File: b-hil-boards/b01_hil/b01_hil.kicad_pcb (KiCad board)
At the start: 2 copper layers, 61.7 x 30.5 mm, 40 parts, among them J1 USB_C_Receptacle_USB2.0, J2 Conn_01x03_Male, U1 ADUM4160, U2 MAX485E, U3 CH340G, Y1 Crystal

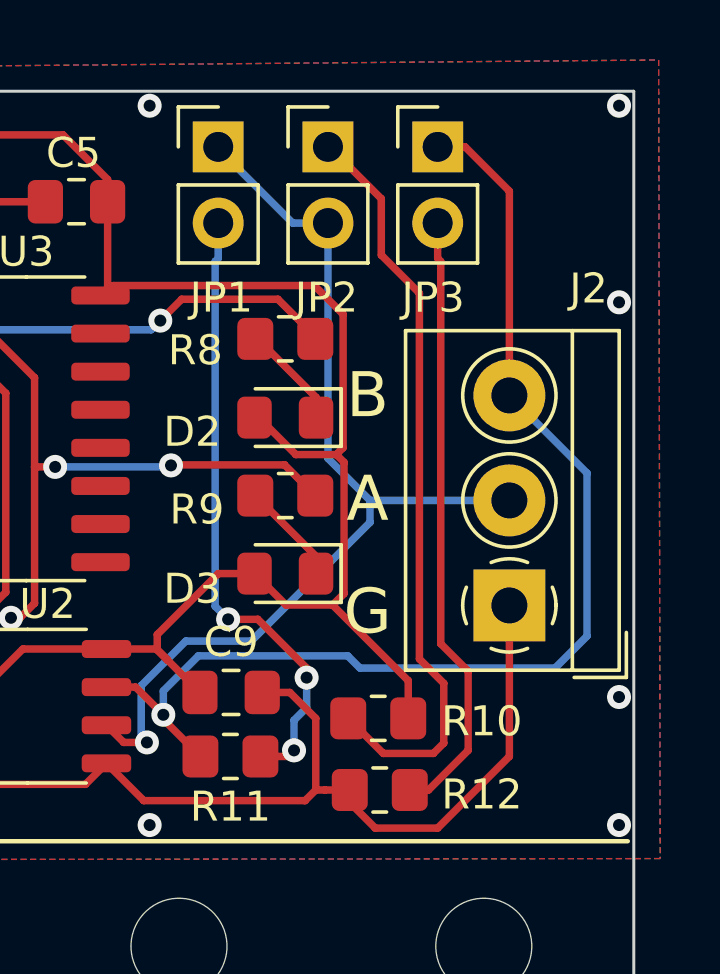
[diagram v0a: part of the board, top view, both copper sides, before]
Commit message: Changed jumper distances to be compatible with 2.54 pin headers
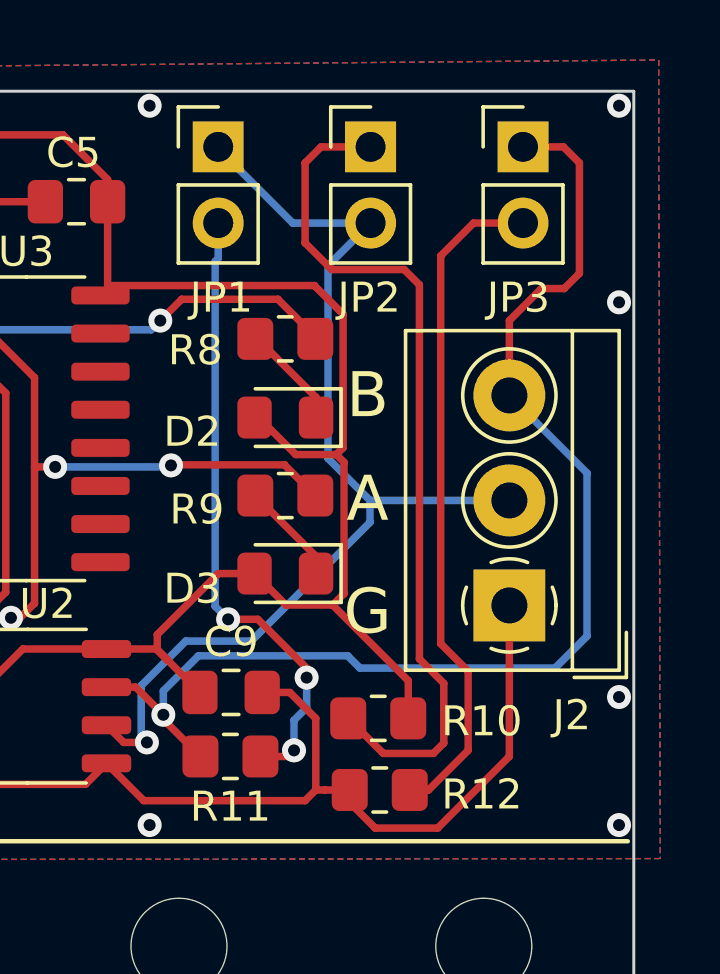
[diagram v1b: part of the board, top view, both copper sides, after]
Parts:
- moved JP3 2.84 mm to (158.0, 101.9)
- moved JP2 1.42 mm to (152.9, 101.9)
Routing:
- net Net-(JP2-Pad1): track 25.3 -> 28.9 mm
- net Net-(JP3-Pad2): track 20.5 -> 22.6 mm
- net /RS485_A: track 33.4 -> 35.4 mm
- net /RS485_B: track 39.1 -> 40.6 mm
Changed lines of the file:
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@@
     (property "Sheetname" "")
     (attr through_hole)
-    (fp_text reference "J2" (at 10.5612 2.64) (layer "F.SilkS")
+    (fp_text reference "J2" (at -3.6628 2.0812) (layer "F.SilkS")
       (effects (font (size 1 1) (thickness 0.15)))
     )
@@
   )
   (footprint "Connector_PinHeader_2.54mm:PinHeader_1x02_P2.54mm_Vertical" (layer "F.Cu")
-    (at 151.4856 101.854)
+    (at 152.908 101.854)
     (descr "Through hole straight pin header, 1x02, 2.54mm pitch, single row")
     (tags "Through hole pin header THT 1x02 2.54mm single row")
@@
   )
   (footprint "Connector_PinHeader_2.54mm:PinHeader_1x02_P2.54mm_Vertical" (layer "F.Cu")
-    (at 155.1432 101.854)
+    (at 157.988 101.854)
     (descr "Through hole straight pin header, 1x02, 2.54mm pitch, single row")
     (tags "Through hole pin header THT 1x02 2.54mm single row")
@@
   (segment (start 148.1578 117.602) (end 147.7264 117.1706) (width 0.25) (layer "B.Cu") (net 36))
   (segment (start 150.7744 120.5484) (end 150.7744 119.5457) (width 0.25) (layer "B.Cu") (net 36))
-  (segment (start 157.5324 103.3288) (end 157.5324 110.1396) (width 0.25) (layer "F.Cu") (net 37))
+  (segment (start 159.8676 106.0704) (end 159.8676 102.3874) (width 0.25) (layer "F.Cu") (net 37))
+  (segment (start 157.5324 110.1396) (end 157.5324 107.6436) (width 0.25) (layer "F.Cu") (net 37))
+  (segment (start 158.5976 106.5784) (end 159.3596 106.5784) (width 0.25) (layer "F.Cu") (net 37))
+  (segment (start 157.5324 107.6436) (end 158.5976 106.5784) (width 0.25) (layer "F.Cu") (net 37))
   (segment (start 145.9979 120.9375) (end 147.2344 122.174) (width 0.25) (layer "F.Cu") (net 37))
-  (segment (start 156.0576 101.854) (end 157.5324 103.3288) (width 0.25) (layer "F.Cu") (net 37))
+  (segment (start 159.8676 102.3874) (end 159.3342 101.854) (width 0.25) (layer "F.Cu") (net 37))
+  (segment (start 159.3596 106.5784) (end 159.8676 106.0704) (width 0.25) (layer "F.Cu") (net 37))
+  (segment (start 159.3342 101.854) (end 157.988 101.854) (width 0.25) (layer "F.Cu") (net 37))
   (segment (start 145.0756 119.8626) (end 145.9979 120.7849) (width 0.25) (layer "F.Cu") (net 37))
   (segment (start 145.9979 120.7849) (end 145.9979 120.9375) (width 0.25) (layer "F.Cu") (net 37))
-  (segment (start 155.1432 101.854) (end 156.0576 101.854) (width 0.25) (layer "F.Cu") (net 37))
   (segment (start 144.103 119.8626) (end 145.0756 119.8626) (width 0.25) (layer "F.Cu") (net 37))
   (via (at 145.9979 120.7849) (size 0.8) (drill 0.4) (layers "F.Cu" "B.Cu") (net 37))
@@
   (segment (start 144.6765 121.7061) (end 145.4508 121.7061) (width 0.25) (layer "F.Cu") (net 38))
   (via (at 145.4508 121.7061) (size 0.8) (drill 0.4) (layers "F.Cu" "B.Cu") (net 38))
-  (segment (start 151.4856 104.394) (end 151.4856 112.2379) (width 0.25) (layer "B.Cu") (net 38))
   (segment (start 145.2607 121.516) (end 145.4508 121.7061) (width 0.25) (layer "B.Cu") (net 38))
   (segment (start 148.9314 118.327) (end 146.7474 118.327) (width 0.25) (layer "B.Cu") (net 38))
   (segment (start 145.2607 119.8137) (end 145.2607 121.516) (width 0.25) (layer "B.Cu") (net 38))
   (segment (start 151.4856 112.2379) (end 152.8873 113.6396) (width 0.25) (layer "B.Cu") (net 38))
+  (segment (start 151.4856 112.2379) (end 151.4856 105.8164) (width 0.25) (layer "B.Cu") (net 38))
   (segment (start 152.8873 114.3711) (end 148.9314 118.327) (width 0.25) (layer "B.Cu") (net 38))
   (segment (start 146.7474 118.327) (end 145.2607 119.8137) (width 0.25) (layer "B.Cu") (net 38))
-  (segment (start 151.4856 104.394) (end 150.3103 104.394) (width 0.25) (layer "B.Cu") (net 38))
+  (segment (start 151.4856 105.8164) (end 152.908 104.394) (width 0.25) (layer "B.Cu") (net 38))
   (segment (start 152.8873 113.6396) (end 152.8873 114.3711) (width 0.25) (layer "B.Cu") (net 38))
   (segment (start 152.8873 113.6396) (end 157.5324 113.6396) (width 0.25) (layer "B.Cu") (net 38))
   (segment (start 147.828 101.9117) (end 147.828 101.854) (width 0.25) (layer "B.Cu") (net 38))
+  (segment (start 150.3103 104.394) (end 152.908 104.394) (width 0.25) (layer "B.Cu") (net 38))
   (segment (start 150.3103 104.394) (end 147.828 101.9117) (width 0.25) (layer "B.Cu") (net 38))
-  (segment (start 154.8384 123.2916) (end 154.2128 123.2916) (width 0.25) (layer "F.Cu") (net 39))
-  (segment (start 155.2448 105.6709) (end 155.2448 118.4148) (width 0.25) (layer "F.Cu") (net 39))
-  (segment (start 155.2448 118.4148) (end 156.1592 119.3292) (width 0.25) (layer "F.Cu") (net 39))
-  (segment (start 156.1592 119.3292) (end 156.1592 121.9708) (width 0.25) (layer "F.Cu") (net 39))
-  (segment (start 155.1432 104.394) (end 155.1432 105.5693) (width 0.25) (layer "F.Cu") (net 39))
-  (segment (start 156.1592 121.9708) (end 154.8384 123.2916) (width 0.25) (layer "F.Cu") (net 39))
-  (segment (start 155.1432 105.5693) (end 155.2448 105.6709) (width 0.25) (layer "F.Cu") (net 39))
-  (segment (start 151.5364 101.854) (end 151.4856 101.854) (width 0.25) (layer "F.Cu") (net 40))
-  (segment (start 154.5336 118.9228) (end 154.5336 106.7308) (width 0.25) (layer "F.Cu") (net 40))
-  (segment (start 154.5336 106.7308) (end 153.2636 105.4608) (width 0.25) (layer "F.Cu") (net 40))
-  (segment (start 153.2636 103.5812) (end 151.5364 101.854) (width 0.25) (layer "F.Cu") (net 40))
+  (segment (start 156.1592 119.3292) (end 155.2448 118.4148) (width 0.25) (layer "F.Cu") (net 39))
+  (segment (start 154.2128 123.2916) (end 154.8384 123.2916) (width 0.25) (layer "F.Cu") (net 39))
+  (segment (start 156.337 104.394) (end 157.988 104.394) (width 0.25) (layer "F.Cu") (net 39))
+  (segment (start 156.1592 121.9708) (end 156.1592 119.3292) (width 0.25) (layer "F.Cu") (net 39))
+  (segment (start 155.2448 105.4862) (end 156.337 104.394) (width 0.25) (layer "F.Cu") (net 39))
+  (segment (start 154.8384 123.2916) (end 156.1592 121.9708) (width 0.25) (layer "F.Cu") (net 39))
+  (segment (start 155.2448 118.4148) (end 155.2448 105.4862) (width 0.25) (layer "F.Cu") (net 39))
   (segment (start 153.3304 122.0724) (end 155.0018 122.0724) (width 0.25) (layer "F.Cu") (net 40))
+  (segment (start 150.7236 102.3874) (end 151.257 101.854) (width 0.25) (layer "F.Cu") (net 40))
+  (segment (start 155.0018 122.0724) (end 155.3464 121.7278) (width 0.25) (layer "F.Cu") (net 40))
+  (segment (start 150.7236 105.0544) (end 150.7236 102.3874) (width 0.25) (layer "F.Cu") (net 40))
+  (segment (start 154.0256 105.9434) (end 151.6126 105.9434) (width 0.25) (layer "F.Cu") (net 40))
+  (segment (start 155.3464 119.7356) (end 154.5336 118.9228) (width 0.25) (layer "F.Cu") (net 40))
+  (segment (start 151.6126 105.9434) (end 150.7236 105.0544) (width 0.25) (layer "F.Cu") (net 40))
+  (segment (start 154.5336 118.9228) (end 154.5336 106.4514) (width 0.25) (layer "F.Cu") (net 40))
+  (segment (start 154.5336 106.4514) (end 154.0256 105.9434) (width 0.25) (layer "F.Cu") (net 40))
   (segment (start 152.162 120.904) (end 153.3304 122.0724) (width 0.25) (layer "F.Cu") (net 40))
-  (segment (start 155.3464 119.7356) (end 154.5336 118.9228) (width 0.25) (layer "F.Cu") (net 40))
+  (segment (start 151.257 101.854) (end 152.908 101.854) (width 0.25) (layer "F.Cu") (net 40))
   (segment (start 155.3464 121.7278) (end 155.3464 119.7356) (width 0.25) (layer "F.Cu") (net 40))
-  (segment (start 155.0018 122.0724) (end 155.3464 121.7278) (width 0.25) (layer "F.Cu") (net 40))
-  (segment (start 153.2636 105.4608) (end 153.2636 103.5812) (width 0.25) (layer "F.Cu") (net 40))
   (zone (net 0) (net_name "") (layers F&B.Cu *.SilkS) (hatch edge 0.508)
     (connect_pads (clearance 0))
